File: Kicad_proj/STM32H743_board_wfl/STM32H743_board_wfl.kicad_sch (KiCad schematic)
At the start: 0 parts

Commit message: v0.1_hierarchy_schematics
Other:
- added sheet 01_Power_Input (power_input.kicad_sch)
- added sheet 02_Power_regulation (power_regulation.kicad_sch)
- added sheet 03_STM32H743_schematic (stm32h743_sch.kicad_sch)
- added sheet 04_BMI088_IMU_sensor (04_bmi088_imu_sensor.kicad_sch)
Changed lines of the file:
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@@
 	(generator_version "10.0")
 	(paper "A4")
+	(sheet
+		(at 89.916 38.608)
+		(size 48.006 37.084)
+		(exclude_from_sim no)
+		(in_bom yes)
+		(on_board yes)
+		(dnp no)
+		(fields_autoplaced yes)
+		(stroke
+			(width 0.1524)
+			(type solid)
+		)
+		(fill
+			(color 0 0 0 0)
+		)
+		(property "Sheetname" "02_Power_regulation"
+			(at 89.916 37.8964 0)
+			(show_name no)
+			(do_not_autoplace no)
+			(effects
+				(font
+					(size 1.27 1.27)
+				)
+				(justify left bottom)
+			)
+		)
+		(property "Sheetfile" "power_regulation.kicad_sch"
+			(at 89.916 76.2766 0)
+			(show_name no)
+			(do_not_autoplace no)
+			(effects
+				(font
+					(size 1.27 1.27)
+				)
+				(justify left top)
+			)
+		)
+		(instances
+			(project "STM32H743_board_wfl"
+				(path "/3ffbaf01-8fe7-4f96-b685-21b9df9d548a"
+					(page "3")
+				)
+			)
+		)
+	)
+	(sheet
+		(at 33.782 38.354)
+		(size 47.498 37.338)
+		(exclude_from_sim no)
+		(in_bom yes)
+		(on_board yes)
+		(dnp no)
+		(fields_autoplaced yes)
+		(stroke
+			(width 0.1524)
+			(type solid)
+		)
+		(fill
+			(color 0 0 0 0)
+		)
+		(property "Sheetname" "01_Power_Input"
+			(at 33.782 37.6424 0)
+			(show_name no)
+			(do_not_autoplace no)
+			(effects
+				(font
+					(size 1.27 1.27)
+				)
+				(justify left bottom)
+			)
+		)
+		(property "Sheetfile" "power_input.kicad_sch"
+			(at 33.782 76.2766 0)
+			(show_name no)
+			(do_not_autoplace no)
+			(effects
+				(font
+					(size 1.27 1.27)
+				)
+				(justify left top)
+			)
+		)
+		(instances
+			(project "STM32H743_board_wfl"
+				(path "/3ffbaf01-8fe7-4f96-b685-21b9df9d548a"
+					(page "2")
+				)
+			)
+		)
+	)
+	(sheet
+		(at 146.304 38.862)
+		(size 48.26 36.83)
+		(exclude_from_sim no)
+		(in_bom yes)
+		(on_board yes)
+		(dnp no)
+		(fields_autoplaced yes)
+		(stroke
+			(width 0.1524)
+			(type solid)
+		)
+		(fill
+			(color 0 0 0 0)
+		)
+		(property "Sheetname" "03_STM32H743_schematic"
+			(at 146.304 38.1504 0)
+			(show_name no)
+			(do_not_autoplace no)
+			(effects
+				(font
+					(size 1.27 1.27)
+				)
+				(justify left bottom)
+			)
+		)
+		(property "Sheetfile" "stm32h743_sch.kicad_sch"
+			(at 146.304 76.2766 0)
+			(show_name no)
+			(do_not_autoplace no)
+			(effects
+				(font
+					(size 1.27 1.27)
+				)
+				(justify left top)
+			)
+		)
+		(instances
+			(project "STM32H743_board_wfl"
+				(path "/3ffbaf01-8fe7-4f96-b685-21b9df9d548a"
+					(page "4")
+				)
+			)
+		)
+	)
+	(sheet
+		(at 204.47 39.37)
+		(size 51.308 36.322)
+		(exclude_from_sim no)
+		(in_bom yes)
+		(on_board yes)
+		(dnp no)
+		(fields_autoplaced yes)
+		(stroke
+			(width 0.1524)
+			(type solid)
+		)
+		(fill
+			(color 0 0 0 0)
+		)
+		(property "Sheetname" "04_BMI088_IMU_sensor"
+			(at 204.47 38.6584 0)
+			(show_name no)
+			(do_not_autoplace no)
+			(effects
+				(font
+					(size 1.27 1.27)
+				)
+				(justify left bottom)
+			)
+		)
+		(property "Sheetfile" "04_bmi088_imu_sensor.kicad_sch"
+			(at 204.47 76.2766 0)
+			(show_name no)
+			(do_not_autoplace no)
+			(effects
+				(font
+					(size 1.27 1.27)
+				)
+				(justify left top)
+			)
+		)
+		(instances
+			(project "STM32H743_board_wfl"
+				(path "/3ffbaf01-8fe7-4f96-b685-21b9df9d548a"
+					(page "5")
+				)
+			)
+		)
+	)
 	(sheet_instances
 		(path "/"

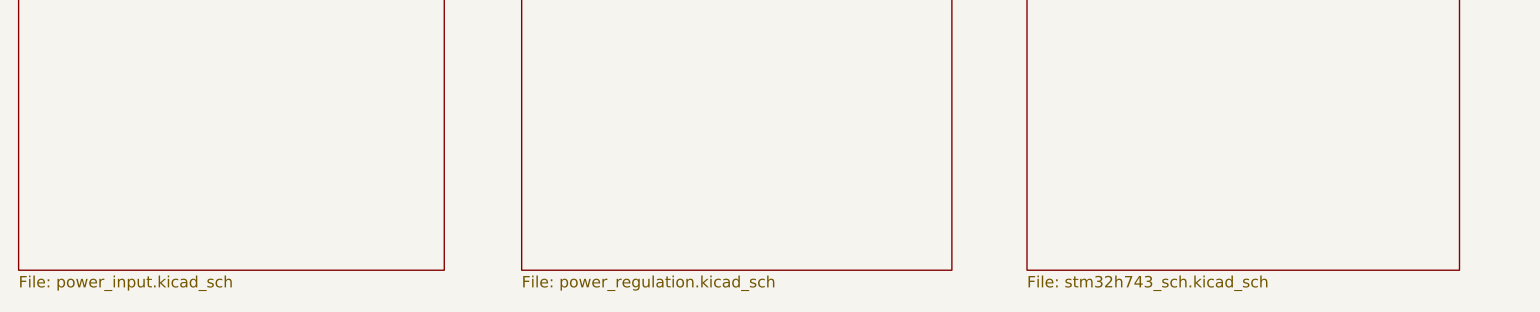
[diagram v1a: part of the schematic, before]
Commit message: schematic filenames update
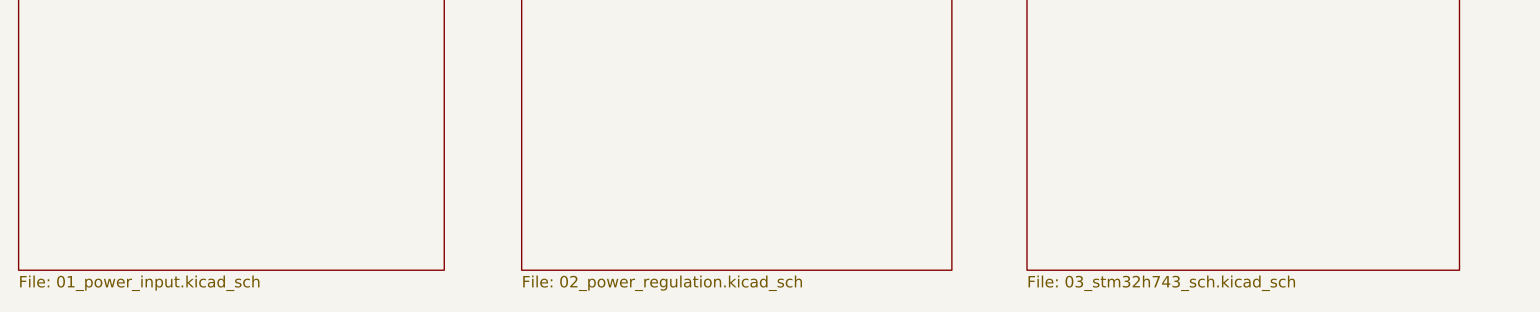
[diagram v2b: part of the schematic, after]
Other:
- sheet 01_Power_Input: file power_input.kicad_sch -> 01_power_input.kicad_sch
- sheet 02_Power_regulation: file power_regulation.kicad_sch -> 02_power_regulation.kicad_sch
- sheet 03_STM32H743_schematic: file stm32h743_sch.kicad_sch -> 03_stm32h743_sch.kicad_sch
- company: (none) -> by wojtron
- title: (none) -> STM32H743 board IMU BMI088 schematics
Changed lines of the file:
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@@
 	(generator_version "10.0")
 	(paper "A4")
+	(title_block
+		(title "STM32H743 board IMU BMI088 schematics")
+		(company "by wojtron")
+	)
 	(sheet
 		(at 89.916 38.608)
@@
 			)
 		)
-		(property "Sheetfile" "power_regulation.kicad_sch"
+		(property "Sheetfile" "02_power_regulation.kicad_sch"
 			(at 89.916 76.2766 0)
 			(show_name no)
@@
 			)
 		)
-		(property "Sheetfile" "power_input.kicad_sch"
+		(property "Sheetfile" "01_power_input.kicad_sch"
 			(at 33.782 76.2766 0)
 			(show_name no)
@@
 			)
 		)
-		(property "Sheetfile" "stm32h743_sch.kicad_sch"
+		(property "Sheetfile" "03_stm32h743_sch.kicad_sch"
 			(at 146.304 76.2766 0)
 			(show_name no)

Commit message: v0.5 schematics + lib update
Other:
- title: STM32H743 board IMU BMI088 schematics -> STM32H743 board with IMU
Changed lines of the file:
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@@
 	(paper "A4")
 	(title_block
-		(title "STM32H743 board IMU BMI088 schematics")
+		(title "STM32H743 board with IMU")
+		(rev "v0.5")
 		(company "by wojtron")
 	)

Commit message: PCB v0.1b connectors
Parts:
- added H1, H2, H3, H4: MountingHole, MountingHole:MountingHole_4mm, symbol Mechanical:MountingHole

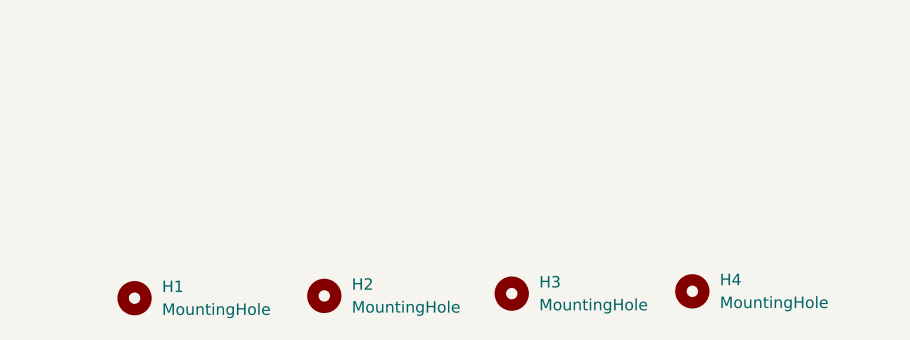
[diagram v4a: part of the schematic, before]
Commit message: PCB v0.1d components placement STM32 caps
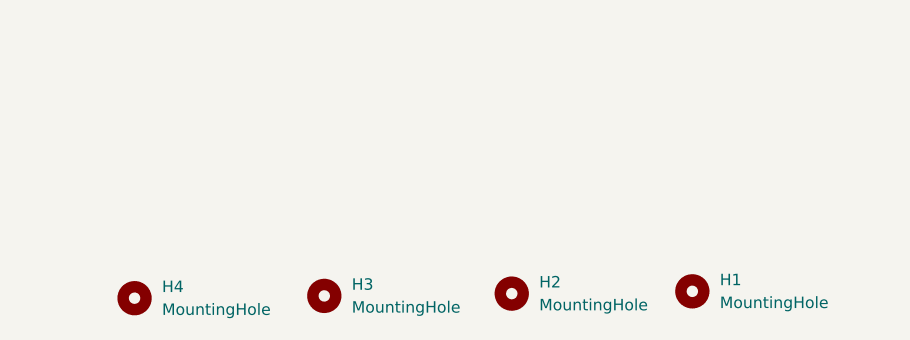
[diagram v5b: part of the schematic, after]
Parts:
- renumbered H4 to H1, H3 to H2, H2 to H3, H1 to H4
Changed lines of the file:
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@@
 		(dnp no)
 		(fields_autoplaced yes)
-		(property "Reference" "H4"
+		(property "Reference" "H1"
 			(at 119.38 175.2599 0)
 			(show_name no)
@@
 			(project "STM32H743_board_wfl"
 				(path "/3ffbaf01-8fe7-4f96-b685-21b9df9d548a"
-					(reference "H4")
+					(reference "H1")
 					(unit 1)
 				)
@@
 		(dnp no)
 		(fields_autoplaced yes)
-		(property "Reference" "H3"
+		(property "Reference" "H2"
 			(at 99.314 175.5139 0)
 			(show_name no)
@@
 			(project "STM32H743_board_wfl"
 				(path "/3ffbaf01-8fe7-4f96-b685-21b9df9d548a"
-					(reference "H3")
+					(reference "H2")
 					(unit 1)
 				)
@@
 		(dnp no)
 		(fields_autoplaced yes)
-		(property "Reference" "H2"
+		(property "Reference" "H3"
 			(at 78.486 175.7679 0)
 			(show_name no)
@@
 			(project "STM32H743_board_wfl"
 				(path "/3ffbaf01-8fe7-4f96-b685-21b9df9d548a"
-					(reference "H2")
+					(reference "H3")
 					(unit 1)
 				)
@@
 		(dnp no)
 		(fields_autoplaced yes)
-		(property "Reference" "H1"
+		(property "Reference" "H4"
 			(at 57.404 176.0219 0)
 			(show_name no)
@@
 			(project "STM32H743_board_wfl"
 				(path "/3ffbaf01-8fe7-4f96-b685-21b9df9d548a"
-					(reference "H1")
-					(unit 1)
-				)
+					(reference "H4")
+					(unit 1)
+				)
